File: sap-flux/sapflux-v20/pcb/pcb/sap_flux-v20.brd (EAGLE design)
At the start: 76.2 x 54.6 mm, 93 parts, among them J1 CON_01X02-0.2"_POL, J2 CON_01X02TINY, J3 CON_01X02TINY, J4 CON_01X02TINY, J5 CON_01X02TINY, Q1 Nfet, Q2 nfet, Q3 pfet, U1 ADP2503, U3 ADP1614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

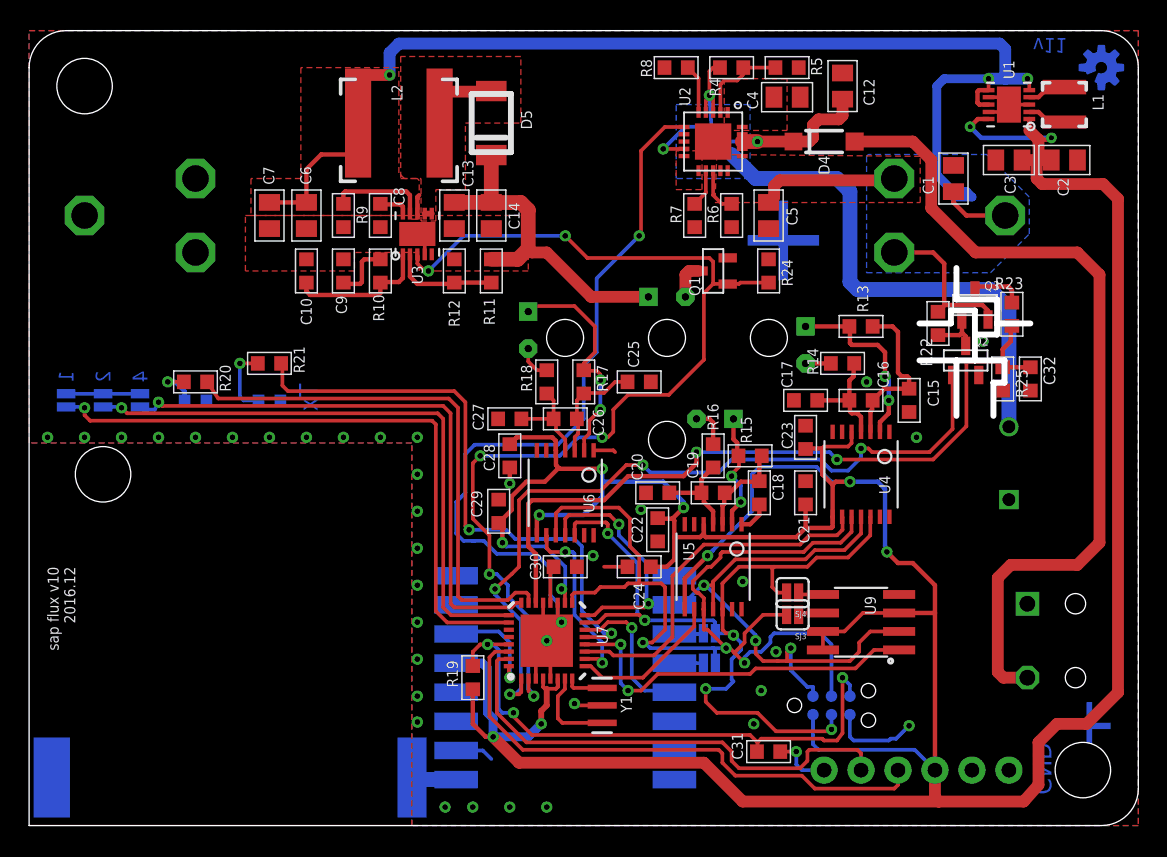
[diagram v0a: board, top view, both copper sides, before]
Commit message: Got the correct time stamp behavior working with reading back storage data
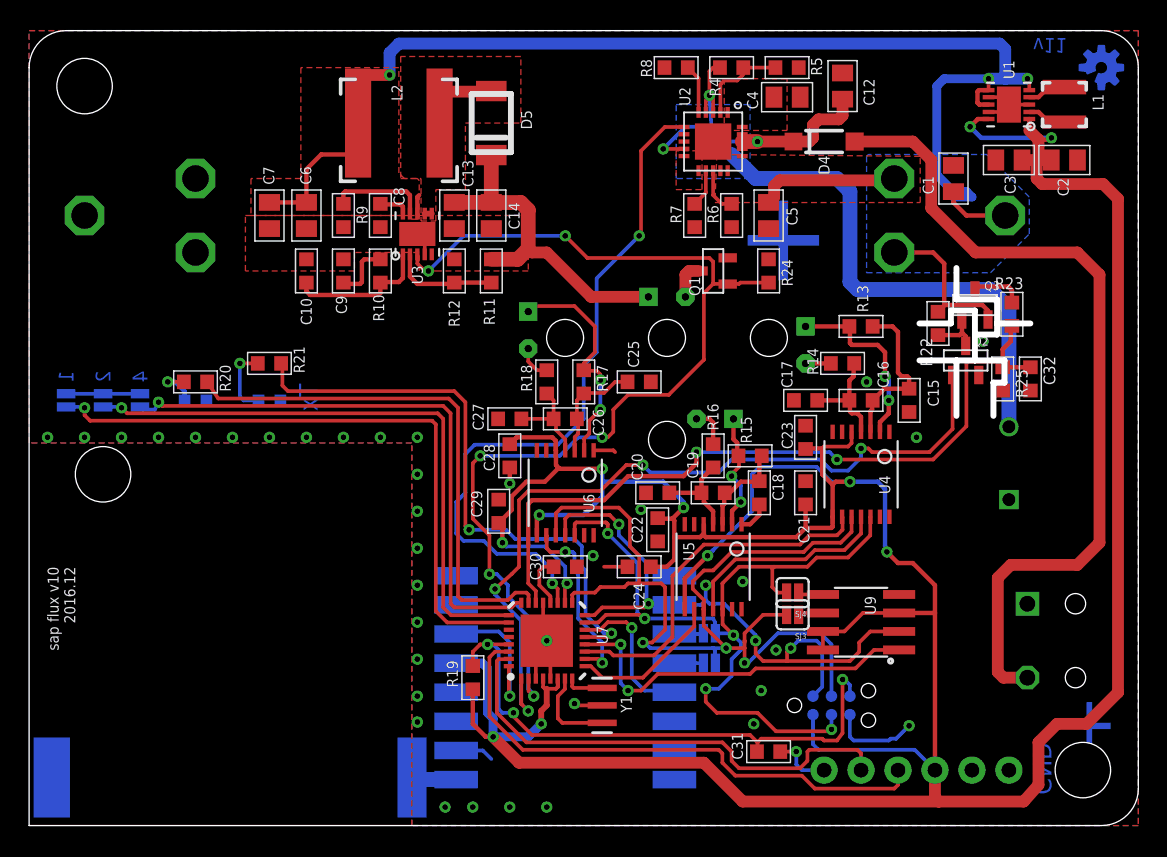
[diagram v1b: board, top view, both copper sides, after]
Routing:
- net PWR_GD: track 51.6 -> 48.6 mm
- net RF_INT: track 7.42 -> 9.96 mm
- net MISO: track 59.0 -> 61.4 mm
- net BAT_V_EN: track 54.3 -> 55.8 mm
- net N$54: track 2.57 -> 3.62 mm
- net MOSI: track 59.0 -> 58.3 mm
- net SCK: track 68.3 -> 67.6 mm

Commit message: added test data
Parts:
- R6: value 10k --CHECK THIS -> I = 1000/R
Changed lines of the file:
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@@
 <attribute name="NAME" x="44.820921875" y="41.36709375" size="0.762" layer="25" font="vector" ratio="18" rot="R90"/>
 </element>
-<element name="R6" library="My_Passives" package="R0603-N" value="10k --CHECK THIS" x="48.26" y="41.91" smashed="yes" rot="R90">
+<element name="R6" library="My_Passives" package="R0603-N" value="I = 1000/R" x="48.26" y="41.91" smashed="yes" rot="R90">
 <attribute name="PARTNO" value="RC0603FR-0710KL" x="48.26" y="41.91" size="1.778" layer="27" font="vector" ratio="15" rot="R90" display="off"/>
 <attribute name="NAME" x="47.360921875" y="41.36709375" size="0.762" layer="25" font="vector" ratio="18" rot="R90"/>

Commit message: checked all part numbers. Minor modifications to bottom text layer
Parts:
- C32: value (none) -> 0.1uF
- R6: value I = 1000/R -> 2k
- R8: value 10k --CHECK THIS -> 10k
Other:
- outline, holes or cut-outs redrawn
- board text added: "Mem"
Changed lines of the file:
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@@
 <text x="1.27" y="17.78" size="0.762" layer="25" font="vector" ratio="18" rot="R270">sap flux v10
 2016.12</text>
-<text x="3.048" y="31.242" size="1.016" layer="16" font="vector" ratio="15" rot="SMR270">1</text>
-<text x="5.588" y="31.242" size="1.016" layer="16" font="vector" ratio="15" rot="SMR270">2</text>
-<text x="8.128" y="31.242" size="1.016" layer="16" font="vector" ratio="15" rot="SMR270">4</text>
-<text x="19.812" y="30.353" size="1.27" layer="16" ratio="15" rot="SMR270">Tx</text>
-<text x="70.231" y="5.715" size="1.27" layer="16" ratio="15" rot="MR270">GND</text>
-<text x="74.803" y="5.207" size="3.81" layer="16" font="vector" ratio="15" rot="MR0">+</text>
+<text x="2.54" y="31.242" size="1.524" layer="16" font="vector" ratio="15" rot="SMR270" align="center">1</text>
+<text x="5.08" y="31.242" size="1.524" layer="16" font="vector" ratio="15" rot="SMR270" align="center">2</text>
+<text x="7.62" y="31.369" size="1.524" layer="16" font="vector" ratio="15" rot="SMR270" align="center">4</text>
+<text x="20.066" y="30.226" size="1.27" layer="16" ratio="15" rot="SMR270">Tx</text>
+<text x="67.818" y="0.635" size="1.27" layer="16" ratio="15" rot="MR0">GND</text>
+<text x="63.373" y="6.731" size="3.81" layer="16" font="vector" ratio="15" rot="MR0">+</text>
 <text x="51.816" y="40.64" size="6.35" layer="16" font="vector" ratio="15" rot="MR0" align="center">+</text>
-<wire x1="63.704809375" y1="28.1432" x2="63.704809375" y2="31.9532" width="0.4064" layer="46"/>
-<wire x1="63.704809375" y1="31.9532" x2="61.164809375" y2="31.9532" width="0.4064" layer="46"/>
-<wire x1="63.704809375" y1="31.9532" x2="64.974809375" y2="31.9532" width="0.4064" layer="46"/>
-<wire x1="64.974809375" y1="31.9532" x2="67.006809375" y2="31.9532" width="0.4064" layer="46"/>
-<wire x1="67.006809375" y1="31.9532" x2="67.006809375" y2="30.4292" width="0.4064" layer="46"/>
-<wire x1="67.006809375" y1="30.4292" x2="66.244809375" y2="30.4292" width="0.4064" layer="46"/>
-<wire x1="66.244809375" y1="30.4292" x2="66.244809375" y2="28.1432" width="0.4064" layer="46"/>
-<wire x1="64.974809375" y1="31.9532" x2="64.974809375" y2="33.7312" width="0.4064" layer="46"/>
-<wire x1="64.974809375" y1="33.7312" x2="64.974809375" y2="35.3822" width="0.4064" layer="46"/>
-<wire x1="64.974809375" y1="35.3822" x2="63.323809375" y2="35.3822" width="0.4064" layer="46"/>
-<wire x1="63.323809375" y1="35.3822" x2="63.323809375" y2="34.4932" width="0.4064" layer="46"/>
-<wire x1="63.323809375" y1="34.4932" x2="61.164809375" y2="34.4932" width="0.4064" layer="46"/>
-<wire x1="63.704809375" y1="38.3032" x2="63.704809375" y2="36.1442" width="0.4064" layer="46"/>
-<wire x1="63.704809375" y1="36.1442" x2="66.498809375" y2="36.1442" width="0.4064" layer="46"/>
-<wire x1="66.498809375" y1="36.1442" x2="66.498809375" y2="34.4932" width="0.4064" layer="46"/>
-<wire x1="66.498809375" y1="34.4932" x2="66.498809375" y2="33.7312" width="0.4064" layer="46"/>
-<wire x1="66.498809375" y1="33.7312" x2="64.974809375" y2="33.7312" width="0.4064" layer="46"/>
-<wire x1="66.498809375" y1="34.4932" x2="68.784809375" y2="34.4932" width="0.4064" layer="46"/>
+<text x="11.938" y="34.163" size="1.27" layer="16" ratio="15" rot="SMR270">Mem</text>
 </plain>
 <attributes>
@@
 <attribute name="NAME" x="44.820921875" y="41.36709375" size="0.762" layer="25" font="vector" ratio="18" rot="R90"/>
 </element>
-<element name="R6" library="My_Passives" package="R0603-N" value="I = 1000/R" x="48.26" y="41.91" smashed="yes" rot="R90">
-<attribute name="PARTNO" value="RC0603FR-0710KL" x="48.26" y="41.91" size="1.778" layer="27" font="vector" ratio="15" rot="R90" display="off"/>
+<element name="R6" library="My_Passives" package="R0603-N" value="2k" x="48.26" y="41.91" smashed="yes" rot="R90">
+<attribute name="PARTNO" value="RC0603FR-072KL" x="48.26" y="41.91" size="1.778" layer="27" font="vector" ratio="15" rot="R90" display="off"/>
 <attribute name="NAME" x="47.360921875" y="41.36709375" size="0.762" layer="25" font="vector" ratio="18" rot="R90"/>
 </element>
-<element name="R8" library="My_Passives" package="R0603-N" value="10k --CHECK THIS" x="44.45" y="52.07" smashed="yes">
+<element name="R8" library="My_Passives" package="R0603-N" value="10k" x="44.45" y="52.07" smashed="yes">
 <attribute name="PARTNO" value="RC0603FR-0710KL" x="44.45" y="52.07" size="1.778" layer="27" font="vector" ratio="15" display="off"/>
 <attribute name="NAME" x="42.788921875" y="51.40009375" size="0.762" layer="25" font="vector" ratio="18" rot="R90"/>
@@
 </element>
 <element name="Q2" library="My_Descrete_Semiconductors" package="SOT23-3" value="nfet" x="64.339809375" y="31.9532" smashed="yes">
-<attribute name="PARTNO" value="" x="64.339809375" y="31.9532" size="1.778" layer="27" display="off"/>
+<attribute name="PARTNO" value="BSS138" x="64.339809375" y="31.9532" size="1.778" layer="27" display="off"/>
 <attribute name="NAME" x="64.847809375" y="32.9692" size="0.6096" layer="25"/>
 <attribute name="VALUE" x="62.434809375" y="29.4132" size="0.6096" layer="27"/>
 </element>
 <element name="Q3" library="My_Descrete_Semiconductors" package="SOT23-3" value="pfet" x="64.974809375" y="35.7632" smashed="yes">
-<attribute name="PARTNO" value="" x="64.974809375" y="35.7632" size="1.778" layer="27" display="off"/>
+<attribute name="PARTNO" value="IRLML2244TRPBF" x="64.974809375" y="35.7632" size="1.778" layer="27" display="off"/>
 <attribute name="NAME" x="65.609809375" y="36.7792" size="0.6096" layer="25"/>
 <attribute name="VALUE" x="63.069809375" y="33.2232" size="0.6096" layer="27"/>
 </element>
 <element name="R22" library="My_Passives" package="R0603-N" value="100k" x="62.434809375" y="34.4932" smashed="yes" rot="R90">
-<attribute name="PARTNO" value="" x="62.434809375" y="34.4932" size="1.778" layer="27" rot="R90" display="off"/>
+<attribute name="PARTNO" value="RC0603FR-07100KL" x="62.434809375" y="34.4932" size="1.778" layer="27" rot="R90" display="off"/>
 <attribute name="NAME" x="62.04373125" y="31.53729375" size="0.8128" layer="25" font="vector" ratio="13" rot="R90"/>
 </element>
 <element name="R23" library="My_Passives" package="R0603-N" value="2.2k" x="67.514809375" y="35.1282" smashed="yes" rot="R90">
-<attribute name="PARTNO" value="" x="67.514809375" y="35.1282" size="1.778" layer="27" rot="R90" display="off"/>
+<attribute name="PARTNO" value="RC0603FR-072K2L" x="67.514809375" y="35.1282" size="1.778" layer="27" rot="R90" display="off"/>
 <attribute name="NAME" x="68.311715625" y="37.658121875" size="0.8128" layer="25" font="vector" ratio="13" rot="R180"/>
 </element>
 <element name="R25" library="My_Passives" package="R0603-N" value="4.7k" x="66.879809375" y="30.6832" smashed="yes" rot="R90">
-<attribute name="PARTNO" value="" x="66.879809375" y="30.6832" size="1.778" layer="27" rot="R90" display="off"/>
+<attribute name="PARTNO" value="RC0603FR-074K7L" x="66.879809375" y="30.6832" size="1.778" layer="27" rot="R90" display="off"/>
 <attribute name="NAME" x="67.7788875" y="31.35310625" size="0.8128" layer="25" font="vector" ratio="13" rot="R270"/>
 </element>
-<element name="C32" library="My_Passives" package="C0603-N" value="" x="68.784809375" y="30.6832" rot="R270">
-<attribute name="PARTNO" value="" x="68.784809375" y="30.6832" size="1.778" layer="27" font="vector" ratio="15" rot="R270" display="off"/>
+<element name="C32" library="My_Passives" package="C0603-N" value="0.1uF" x="68.784809375" y="30.6832" rot="R270">
+<attribute name="PARTNO" value="CC0603KRX7R7BB104" x="68.784809375" y="30.6832" size="1.778" layer="27" font="vector" ratio="15" rot="R270" display="off"/>
 </element>
 <element name="SJ1" library="My_Connectors" package="SJ_2S" value="SOLDERJUMPERNC" x="46.736" y="11.176" rot="MR0">
-<attribute name="PARTNO" value="" x="46.736" y="11.176" size="1.778" layer="28" font="vector" ratio="15" rot="MR0" display="off"/>
+<attribute name="PARTNO" value="NA" x="46.736" y="11.176" size="1.778" layer="28" font="vector" ratio="15" rot="MR0" display="off"/>
 </element>
 <element name="SJ2" library="My_Connectors" package="SJ_2S" value="SOLDERJUMPERNC" x="46.736" y="13.208" rot="MR0">
-<attribute name="PARTNO" value="" x="46.736" y="13.208" size="1.778" layer="28" font="vector" ratio="15" rot="MR0" display="off"/>
+<attribute name="PARTNO" value="NA" x="46.736" y="13.208" size="1.778" layer="28" font="vector" ratio="15" rot="MR0" display="off"/>
 </element>
 <element name="SJ3" library="My_Connectors" package="SJ_2S" value="SOLDERJUMPERNC" x="52.451" y="14.478" rot="R180">
-<attribute name="PARTNO" value="" x="52.451" y="14.478" size="1.778" layer="27" font="vector" ratio="15" rot="R180" display="off"/>
+<attribute name="PARTNO" value="NA" x="52.451" y="14.478" size="1.778" layer="27" font="vector" ratio="15" rot="R180" display="off"/>
 </element>
 <element name="SJ4" library="My_Connectors" package="SJ_2S" value="SOLDERJUMPERNC" x="52.451" y="16.002" rot="R180">
-<attribute name="PARTNO" value="" x="52.451" y="16.002" size="1.778" layer="27" font="vector" ratio="15" rot="R180" display="off"/>
+<attribute name="PARTNO" value="NA" x="52.451" y="16.002" size="1.778" layer="27" font="vector" ratio="15" rot="R180" display="off"/>
 </element>
 </elements>
